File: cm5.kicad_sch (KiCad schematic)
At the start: 6 parts, among them J1 Conn_01x03, U2 10164227-1001A1RLF, U3 10164227-1001A1RLF

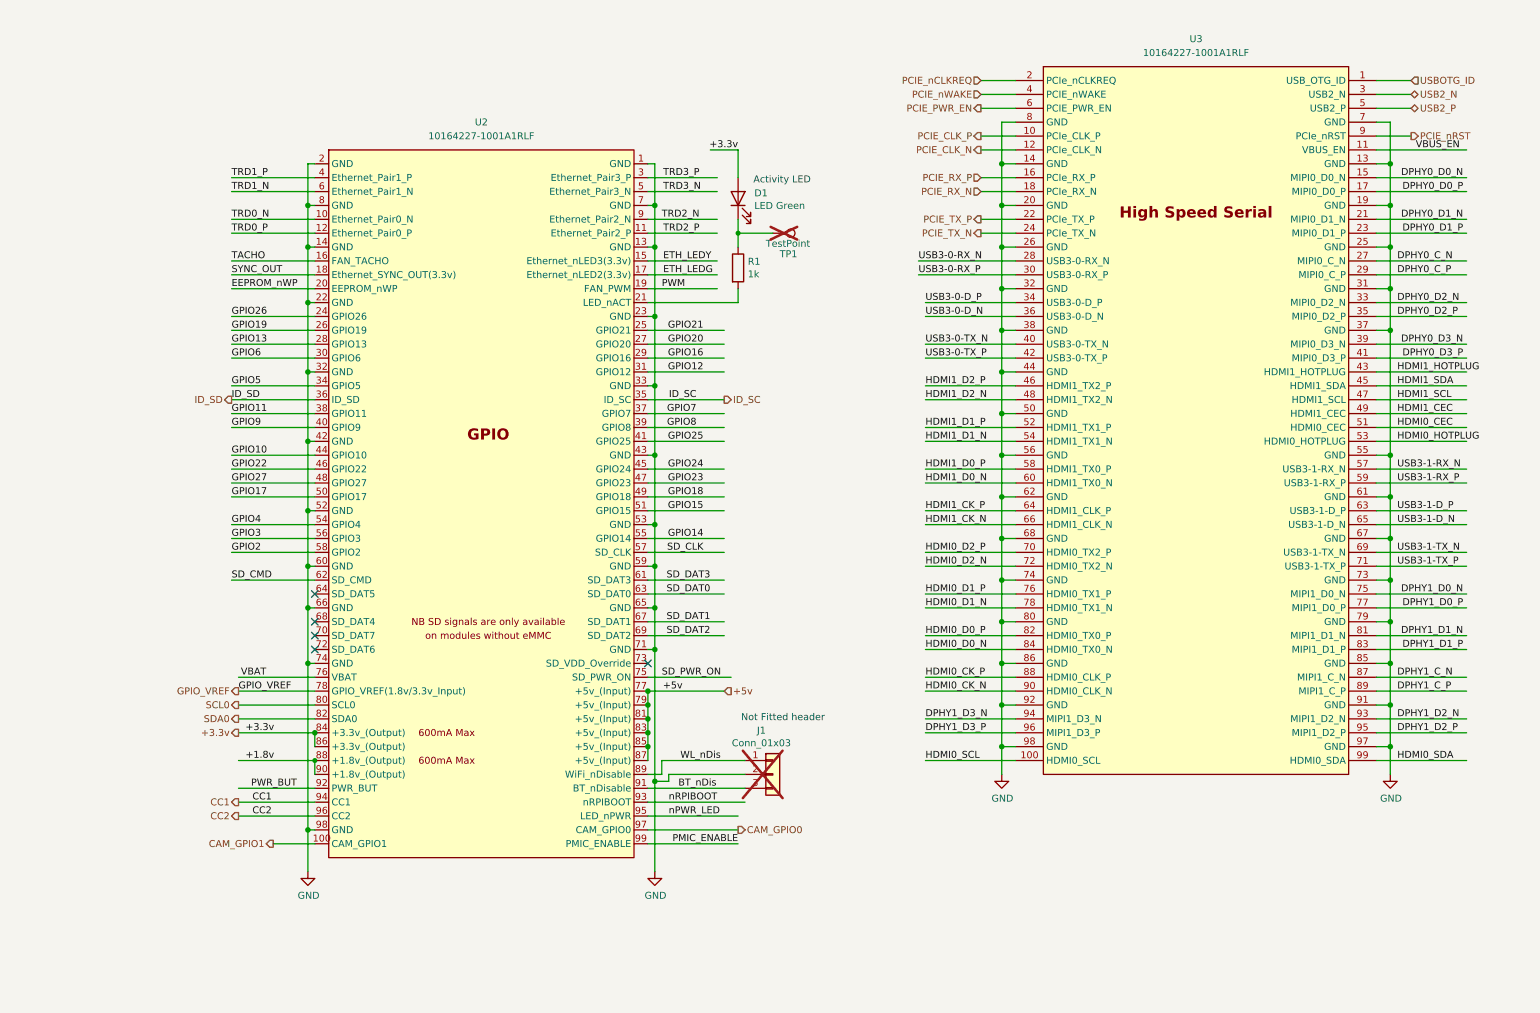
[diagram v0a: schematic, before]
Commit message: added m2 mkey conn, defined signals
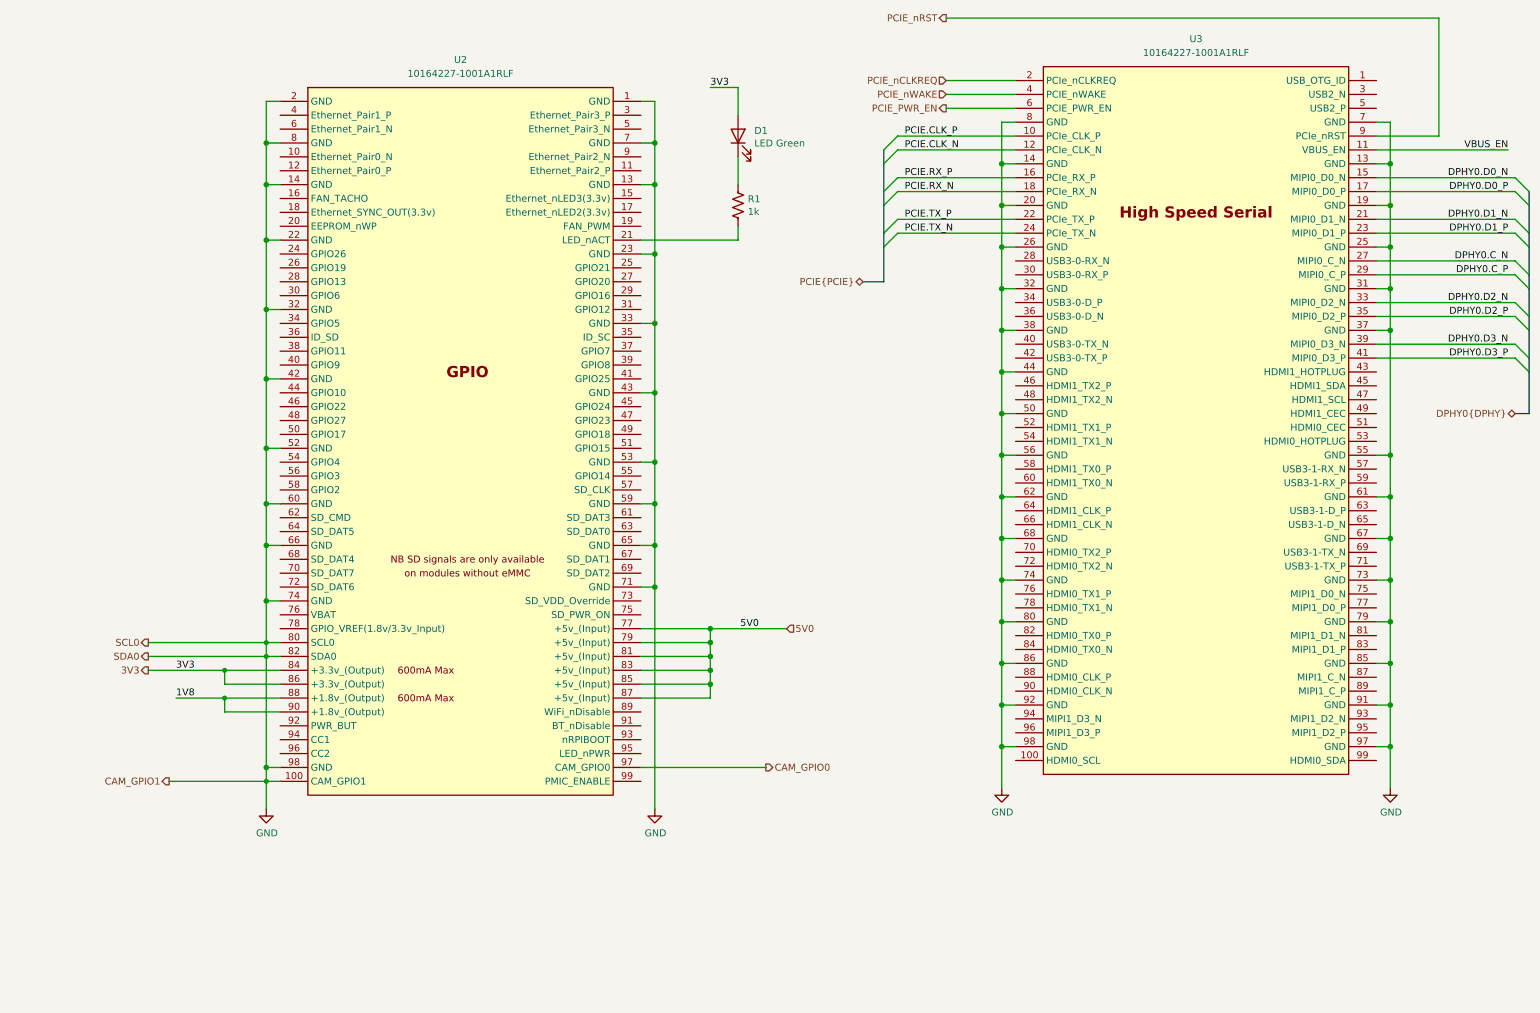
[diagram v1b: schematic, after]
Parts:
- removed J1: Conn_01x03, Connector_PinHeader_2.54mm:PinHeader_1x03_P2.54mm_Vertical, symbol Connector_Generic:Conn_01x03
- removed TP1: TestPoint, TestPoint:TestPoint_Pad_2.0x2.0mm, symbol Connector:TestPoint
- R1: symbol Device:R -> Device:R_US
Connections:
- net CAM_GPIO1 is gone; now on net GND: U2.100 (CAM_GPIO1)
- net SCL0 is gone; now on net GND: U2.80 (SCL0)
- net SDA0 is gone; now on net GND: U2.82 (SDA0)
- net +1.8v renamed 1V8
- net +3.3v renamed 3V3
- net +5v renamed 5V0
- net BT_nDis: no longer names the net of U2.91 (BT_nDisable)
- net CC1: no longer names the net of U2.94 (CC1)
- net CC2: no longer names the net of U2.96 (CC2)
- net DPHY0_C_N renamed DPHY0.C_N
- net DPHY0_C_P renamed DPHY0.C_P
- net DPHY0_D0_N renamed DPHY0.D0_N
- net DPHY0_D0_P renamed DPHY0.D0_P
- net DPHY0_D1_N renamed DPHY0.D1_N
- net DPHY0_D1_P renamed DPHY0.D1_P
- net DPHY0_D2_N renamed DPHY0.D2_N
- net DPHY0_D2_P renamed DPHY0.D2_P
- net DPHY0_D3_N renamed DPHY0.D3_N
- net DPHY0_D3_P renamed DPHY0.D3_P
- net DPHY1_C_N: no longer names the net of U3.87 (MIPI1_C_N)
- net DPHY1_C_P: no longer names the net of U3.89 (MIPI1_C_P)
- net DPHY1_D0_N: no longer names the net of U3.75 (MIPI1_D0_N)
- net DPHY1_D0_P: no longer names the net of U3.77 (MIPI1_D0_P)
- net DPHY1_D1_N: no longer names the net of U3.81 (MIPI1_D1_N)
- net DPHY1_D1_P: no longer names the net of U3.83 (MIPI1_D1_P)
- net DPHY1_D2_N: no longer names the net of U3.93 (MIPI1_D2_N)
- net DPHY1_D2_P: no longer names the net of U3.95 (MIPI1_D2_P)
- net DPHY1_D3_N: no longer names the net of U3.94 (MIPI1_D3_N)
- net DPHY1_D3_P: no longer names the net of U3.96 (MIPI1_D3_P)
- net EEPROM_nWP: no longer names the net of U2.20 (EEPROM_nWP)
- net ETH_LEDG: no longer names the net of U2.17 (Ethernet_nLED2(3.3v))
- net ETH_LEDY: no longer names the net of U2.15 (Ethernet_nLED3(3.3v))
- net GPIO10: no longer names the net of U2.44 (GPIO10)
- net GPIO11: no longer names the net of U2.38 (GPIO11)
- net GPIO12: no longer names the net of U2.31 (GPIO12)
- net GPIO13: no longer names the net of U2.28 (GPIO13)
- net GPIO14: no longer names the net of U2.55 (GPIO14)
- net GPIO15: no longer names the net of U2.51 (GPIO15)
- net GPIO16: no longer names the net of U2.29 (GPIO16)
- net GPIO17: no longer names the net of U2.50 (GPIO17)
- net GPIO18: no longer names the net of U2.49 (GPIO18)
- net GPIO19: no longer names the net of U2.26 (GPIO19)
- net GPIO2: no longer names the net of U2.58 (GPIO2)
- net GPIO20: no longer names the net of U2.27 (GPIO20)
- net GPIO21: no longer names the net of U2.25 (GPIO21)
- net GPIO22: no longer names the net of U2.46 (GPIO22)
- net GPIO23: no longer names the net of U2.47 (GPIO23)
- net GPIO24: no longer names the net of U2.45 (GPIO24)
- net GPIO25: no longer names the net of U2.41 (GPIO25)
- net GPIO26: no longer names the net of U2.24 (GPIO26)
- net GPIO27: no longer names the net of U2.48 (GPIO27)
- net GPIO3: no longer names the net of U2.56 (GPIO3)
- net GPIO4: no longer names the net of U2.54 (GPIO4)
- net GPIO5: no longer names the net of U2.34 (GPIO5)
- net GPIO6: no longer names the net of U2.30 (GPIO6)
- net GPIO7: no longer names the net of U2.37 (GPIO7)
- net GPIO8: no longer names the net of U2.39 (GPIO8)
- net GPIO9: no longer names the net of U2.40 (GPIO9)
- net GPIO_VREF: no longer names the net of U2.78 (GPIO_VREF(1.8v/3.3v_Input))
- net HDMI0_CEC: no longer names the net of U3.51 (HDMI0_CEC)
- net HDMI0_CK_N: no longer names the net of U3.90 (HDMI0_CLK_N)
- net HDMI0_CK_P: no longer names the net of U3.88 (HDMI0_CLK_P)
- net HDMI0_D0_N: no longer names the net of U3.84 (HDMI0_TX0_N)
- net HDMI0_D0_P: no longer names the net of U3.82 (HDMI0_TX0_P)
- net HDMI0_D1_N: no longer names the net of U3.78 (HDMI0_TX1_N)
- net HDMI0_D1_P: no longer names the net of U3.76 (HDMI0_TX1_P)
- net HDMI0_D2_N: no longer names the net of U3.72 (HDMI0_TX2_N)
- net HDMI0_D2_P: no longer names the net of U3.70 (HDMI0_TX2_P)
- net HDMI0_HOTPLUG: no longer names the net of U3.53 (HDMI0_HOTPLUG)
- net HDMI0_SCL: no longer names the net of U3.100 (HDMI0_SCL)
- net HDMI0_SDA: no longer names the net of U3.99 (HDMI0_SDA)
- net HDMI1_CEC: no longer names the net of U3.49 (HDMI1_CEC)
- net HDMI1_CK_N: no longer names the net of U3.66 (HDMI1_CLK_N)
- net HDMI1_CK_P: no longer names the net of U3.64 (HDMI1_CLK_P)
- net HDMI1_D0_N: no longer names the net of U3.60 (HDMI1_TX0_N)
- net HDMI1_D0_P: no longer names the net of U3.58 (HDMI1_TX0_P)
- net HDMI1_D1_N: no longer names the net of U3.54 (HDMI1_TX1_N)
- net HDMI1_D1_P: no longer names the net of U3.52 (HDMI1_TX1_P)
- net HDMI1_D2_N: no longer names the net of U3.48 (HDMI1_TX2_N)
- net HDMI1_D2_P: no longer names the net of U3.46 (HDMI1_TX2_P)
- net HDMI1_HOTPLUG: no longer names the net of U3.43 (HDMI1_HOTPLUG)
- net HDMI1_SCL: no longer names the net of U3.47 (HDMI1_SCL)
- net HDMI1_SDA: no longer names the net of U3.45 (HDMI1_SDA)
- net ID_SC: no longer names the net of U2.35 (ID_SC)
- net ID_SD: no longer names the net of U2.36 (ID_SD)
- net PCIE_CLK_N renamed PCIE.CLK_N
- net PCIE_CLK_P renamed PCIE.CLK_P
- net PCIE_RX_N renamed PCIE.RX_N
- net PCIE_RX_P renamed PCIE.RX_P
- net PCIE_TX_N renamed PCIE.TX_N
- net PCIE_TX_P renamed PCIE.TX_P
- net PMIC_ENABLE: no longer names the net of U2.99 (PMIC_ENABLE)
- net PWM: no longer names the net of U2.19 (FAN_PWM)
- net PWR_BUT: no longer names the net of U2.92 (PWR_BUT)
- net SD_CLK: no longer names the net of U2.57 (SD_CLK)
- net SD_CMD: no longer names the net of U2.62 (SD_CMD)
- net SD_DAT0: no longer names the net of U2.63 (SD_DAT0)
- net SD_DAT1: no longer names the net of U2.67 (SD_DAT1)
- net SD_DAT2: no longer names the net of U2.69 (SD_DAT2)
- net SD_DAT3: no longer names the net of U2.61 (SD_DAT3)
- net SD_PWR_ON: no longer names the net of U2.75 (SD_PWR_ON)
- net SYNC_OUT: no longer names the net of U2.18 (Ethernet_SYNC_OUT(3.3v))
- net TACHO: no longer names the net of U2.16 (FAN_TACHO)
- net TRD0_N: no longer names the net of U2.10 (Ethernet_Pair0_N)
- net TRD0_P: no longer names the net of U2.12 (Ethernet_Pair0_P)
- net TRD1_N: no longer names the net of U2.6 (Ethernet_Pair1_N)
- net TRD1_P: no longer names the net of U2.4 (Ethernet_Pair1_P)
- net TRD2_N: no longer names the net of U2.9 (Ethernet_Pair2_N)
- net TRD2_P: no longer names the net of U2.11 (Ethernet_Pair2_P)
- net TRD3_N: no longer names the net of U2.5 (Ethernet_Pair3_N)
- net TRD3_P: no longer names the net of U2.3 (Ethernet_Pair3_P)
- net USB2_N: no longer names the net of U3.3 (USB2_N)
- net USB2_P: no longer names the net of U3.5 (USB2_P)
- net USB3-0-D_N: no longer names the net of U3.36 (USB3-0-D_N)
- net USB3-0-D_P: no longer names the net of U3.34 (USB3-0-D_P)
- net USB3-0-RX_N: no longer names the net of U3.28 (USB3-0-RX_N)
- net USB3-0-RX_P: no longer names the net of U3.30 (USB3-0-RX_P)
- net USB3-0-TX_N: no longer names the net of U3.40 (USB3-0-TX_N)
- net USB3-0-TX_P: no longer names the net of U3.42 (USB3-0-TX_P)
- net USB3-1-D_N: no longer names the net of U3.65 (USB3-1-D_N)
- net USB3-1-D_P: no longer names the net of U3.63 (USB3-1-D_P)
- net USB3-1-RX_N: no longer names the net of U3.57 (USB3-1-RX_N)
- net USB3-1-RX_P: no longer names the net of U3.59 (USB3-1-RX_P)
- net USB3-1-TX_N: no longer names the net of U3.69 (USB3-1-TX_N)
- net USB3-1-TX_P: no longer names the net of U3.71 (USB3-1-TX_P)
- net USBOTG_ID: no longer names the net of U3.1 (USB_OTG_ID)
- net VBAT: no longer names the net of U2.76 (VBAT)
- net WL_nDis: no longer names the net of U2.89 (WiFi_nDisable)
- net nPWR_LED: no longer names the net of U2.95 (LED_nPWR)
- net nRPIBOOT: no longer names the net of U2.93 (nRPIBOOT)
- no-connect marks 5 -> 0
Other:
- note removed: "Activity LED"
- note removed: "Not Fitted header"
- moved on the sheet: D1, U2

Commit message: restructured symbols, added footprints
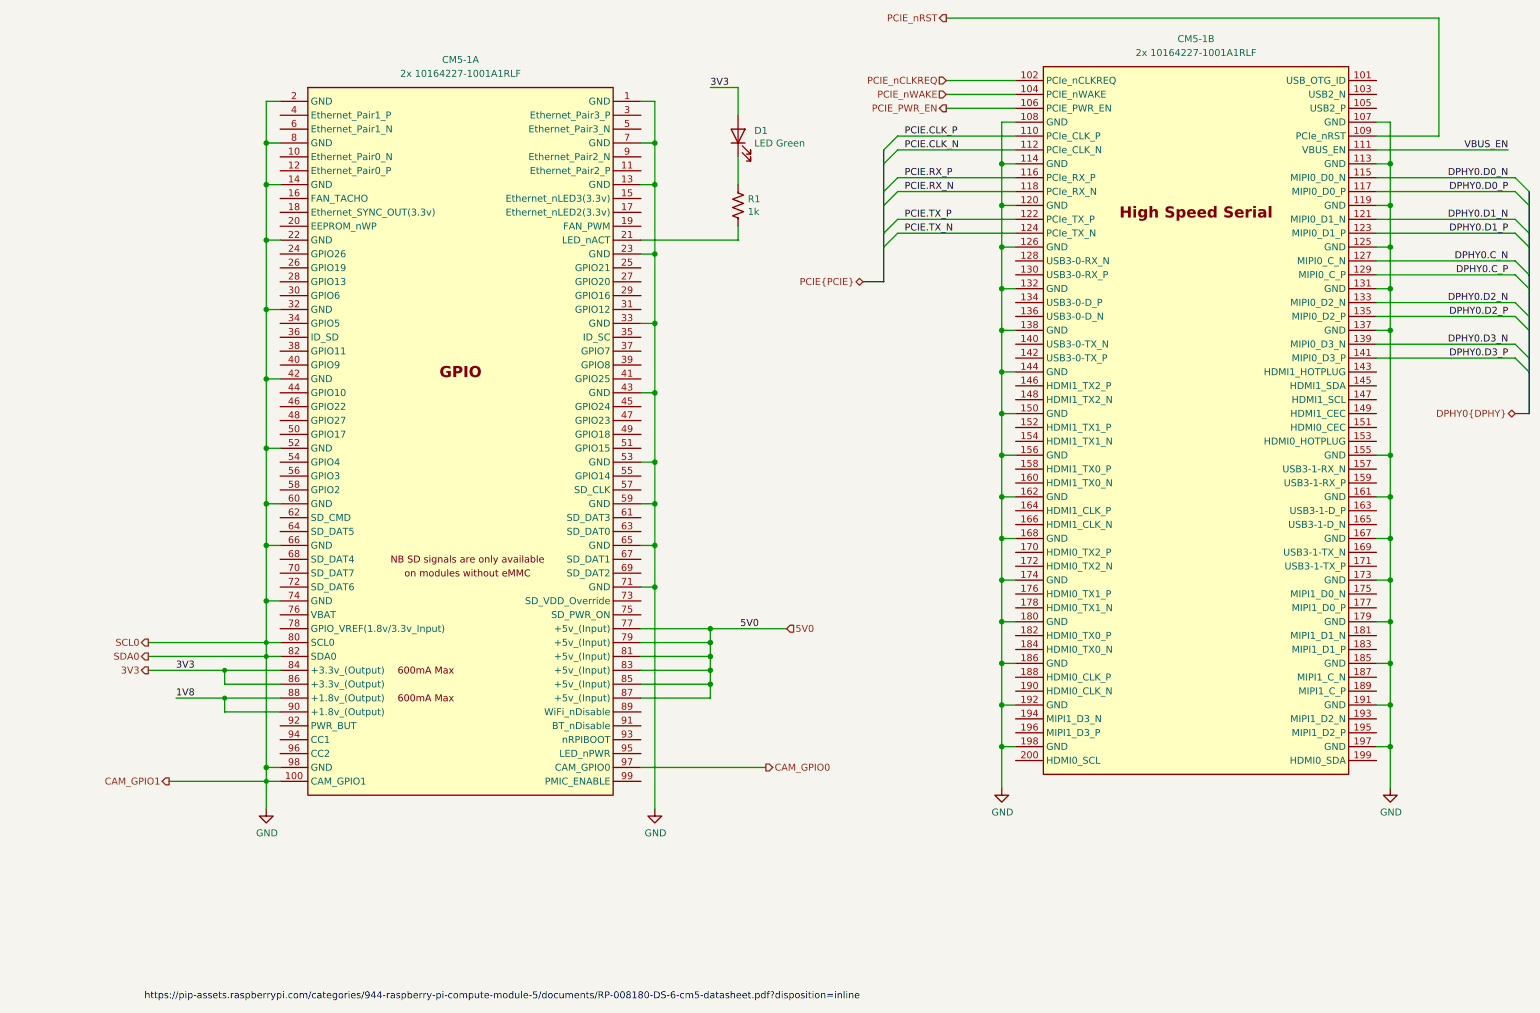
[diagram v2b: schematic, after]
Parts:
- removed U2, U3: 10164227-1001A1RLF, symbol library:10164227-1001A1RLF
- added CM5-1: 2x 10164227-1001A1RLF, library:RPi-CM5, symbol library:CM5
- D1: symbol Device:LED -> library:LED
- R1: symbol Device:R_US -> library:R_US
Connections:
- net 1V8: now also CM5-1.88 (+1.8v_(Output)), CM5-1.90 (+1.8v_(Output))
- net 3V3: now also CM5-1.84 (+3.3v_(Output)), CM5-1.86 (+3.3v_(Output))
- net 5V0: now also CM5-1.77 (+5v_(Input)), CM5-1.79 (+5v_(Input)), CM5-1.81 (+5v_(Input)), CM5-1.83 (+5v_(Input)), CM5-1.85 (+5v_(Input)), CM5-1.87 (+5v_(Input))
- net CAM_GPIO0: now also CM5-1.97 (CAM_GPIO0)
- net DPHY0.C_N: now also CM5-1.127 (MIPI0_C_N)
- net DPHY0.C_P: now also CM5-1.129 (MIPI0_C_P)
- net DPHY0.D0_N: now also CM5-1.115 (MIPI0_D0_N)
- net DPHY0.D0_P: now also CM5-1.117 (MIPI0_D0_P)
- net DPHY0.D1_N: now also CM5-1.121 (MIPI0_D1_N)
- net DPHY0.D1_P: now also CM5-1.123 (MIPI0_D1_P)
- net DPHY0.D2_N: now also CM5-1.133 (MIPI0_D2_N)
- net DPHY0.D2_P: now also CM5-1.135 (MIPI0_D2_P)
- net DPHY0.D3_N: now also CM5-1.139 (MIPI0_D3_N)
- net DPHY0.D3_P: now also CM5-1.141 (MIPI0_D3_P)
- net GND: now also CM5-1.1 (GND), CM5-1.100 (CAM_GPIO1), CM5-1.107 (GND), CM5-1.108 (GND), CM5-1.113 (GND), CM5-1.114 (GND), CM5-1.119 (GND), CM5-1.120 (GND), CM5-1.125 (GND), CM5-1.126 (GND), CM5-1.13 (GND), CM5-1.131 (GND), CM5-1.132 (GND), CM5-1.137 (GND), CM5-1.138 (GND), CM5-1.14 (GND), CM5-1.144 (GND), CM5-1.150 (GND), CM5-1.155 (GND), CM5-1.156 (GND), CM5-1.161 (GND), CM5-1.162 (GND), CM5-1.167 (GND), CM5-1.168 (GND), CM5-1.173 (GND), CM5-1.174 (GND), CM5-1.179 (GND), CM5-1.180 (GND), CM5-1.185 (GND), CM5-1.186 (GND), CM5-1.191 (GND), CM5-1.192 (GND), CM5-1.197 (GND), CM5-1.198 (GND), CM5-1.2 (GND), CM5-1.22 (GND), CM5-1.23 (GND), CM5-1.32 (GND), CM5-1.33 (GND), CM5-1.42 (GND), CM5-1.43 (GND), CM5-1.52 (GND), CM5-1.53 (GND), CM5-1.59 (GND), CM5-1.60 (GND), CM5-1.65 (GND), CM5-1.66 (GND), CM5-1.7 (GND), CM5-1.71 (GND), CM5-1.74 (GND), CM5-1.8 (GND), CM5-1.80 (SCL0), CM5-1.82 (SDA0), CM5-1.98 (GND)
- net PCIE.CLK_N: now also CM5-1.112 (PCIe_CLK_N)
- net PCIE.CLK_P: now also CM5-1.110 (PCIe_CLK_P)
- net PCIE.RX_N: now also CM5-1.118 (PCIe_RX_N)
- net PCIE.RX_P: now also CM5-1.116 (PCIe_RX_P)
- net PCIE.TX_N: now also CM5-1.124 (PCIe_TX_N)
- net PCIE.TX_P: now also CM5-1.122 (PCIe_TX_P)
- net PCIE_PWR_EN: now also CM5-1.106 (PCIE_PWR_EN)
- net PCIE_nCLKREQ: now also CM5-1.102 (PCIe_nCLKREQ)
- net PCIE_nRST: now also CM5-1.109 (PCIe_nRST)
- net PCIE_nWAKE: now also CM5-1.104 (PCIE_nWAKE)
- net VBUS_EN: now also CM5-1.111 (VBUS_EN)
- net at R1.2: now also CM5-1.21 (LED_nACT)
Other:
- note added: "https://pip-assets.raspberrypi.com/categories/944-raspberry-pi-compute-module-5/documents/RP-008180-DS-6-cm5-datasheet.pdf?disposition=inline"

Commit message: quick push, no major change
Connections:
- net 1V8: no longer names the net of CM5-1.88 (+1.8v_(Output))
- net 1V8: no longer CM5-1.90 (+1.8v_(Output))
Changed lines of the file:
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@@
-	)
-	(junction
-		(at 40.64 140.97)
-		(diameter 0)
-		(color 0 0 0 0)
 	)
 	(junction
@@
 	(wire
 		(pts
-			(xy 31.75 140.97) (xy 40.64 140.97)
-		)
-		(stroke
-			(width 0)
-			(type solid)
-		)
-	)
-	(wire
-		(pts
 			(xy 48.26 69.85) (xy 50.8 69.85)
 		)
@@
 	(wire
 		(pts
-			(xy 40.64 143.51) (xy 50.8 143.51)
-		)
-		(stroke
-			(width 0)
-			(type solid)
-		)
-	)
-	(wire
-		(pts
 			(xy 129.54 29.21) (xy 134.62 29.21)
 		)
@@
 		)
 	)
-	(wire
-		(pts
-			(xy 40.64 140.97) (xy 50.8 140.97)
-		)
-		(stroke
-			(width 0)
-			(type solid)
-		)
-	)
 	(bus
 		(pts
@@
 		(pts
 			(xy 182.88 81.28) (xy 185.42 81.28)
-		)
-		(stroke
-			(width 0)
-			(type solid)
-		)
-	)
-	(wire
-		(pts
-			(xy 40.64 143.51) (xy 40.64 140.97)
 		)
 		(stroke
@@
 		(effects
 			(font
-				(size 1.27 1.27)
-			)
-			(justify left bottom)
-		)
-	)
-	(label "1V8"
-		(at 31.75 140.97 0)
-		(effects
-			(font
